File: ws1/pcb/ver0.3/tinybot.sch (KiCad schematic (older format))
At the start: 20 parts, among them IC1 ATTINY84-P, P1 PWR, P2 Pin Breakout, P3 ICSP, P4 M1, P5 M2, U1 LD1117S33TR, U2 L293D

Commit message: switching to DRV8835
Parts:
- removed U2: L293D, Housings_SOIC:SOIC-16_7.5x10.3mm_Pitch1.27mm, symbol L293D
- added U?: DRV8835, symbol DRV8835
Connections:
- net labels added: MODE, PH1, PH2
- wire segments 110 -> 92
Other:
- note added: "DRV8835 disconnect jumper."
- note removed: "L293D disconnect jumper."
- moved on the sheet: JP2, P3, P4, P5

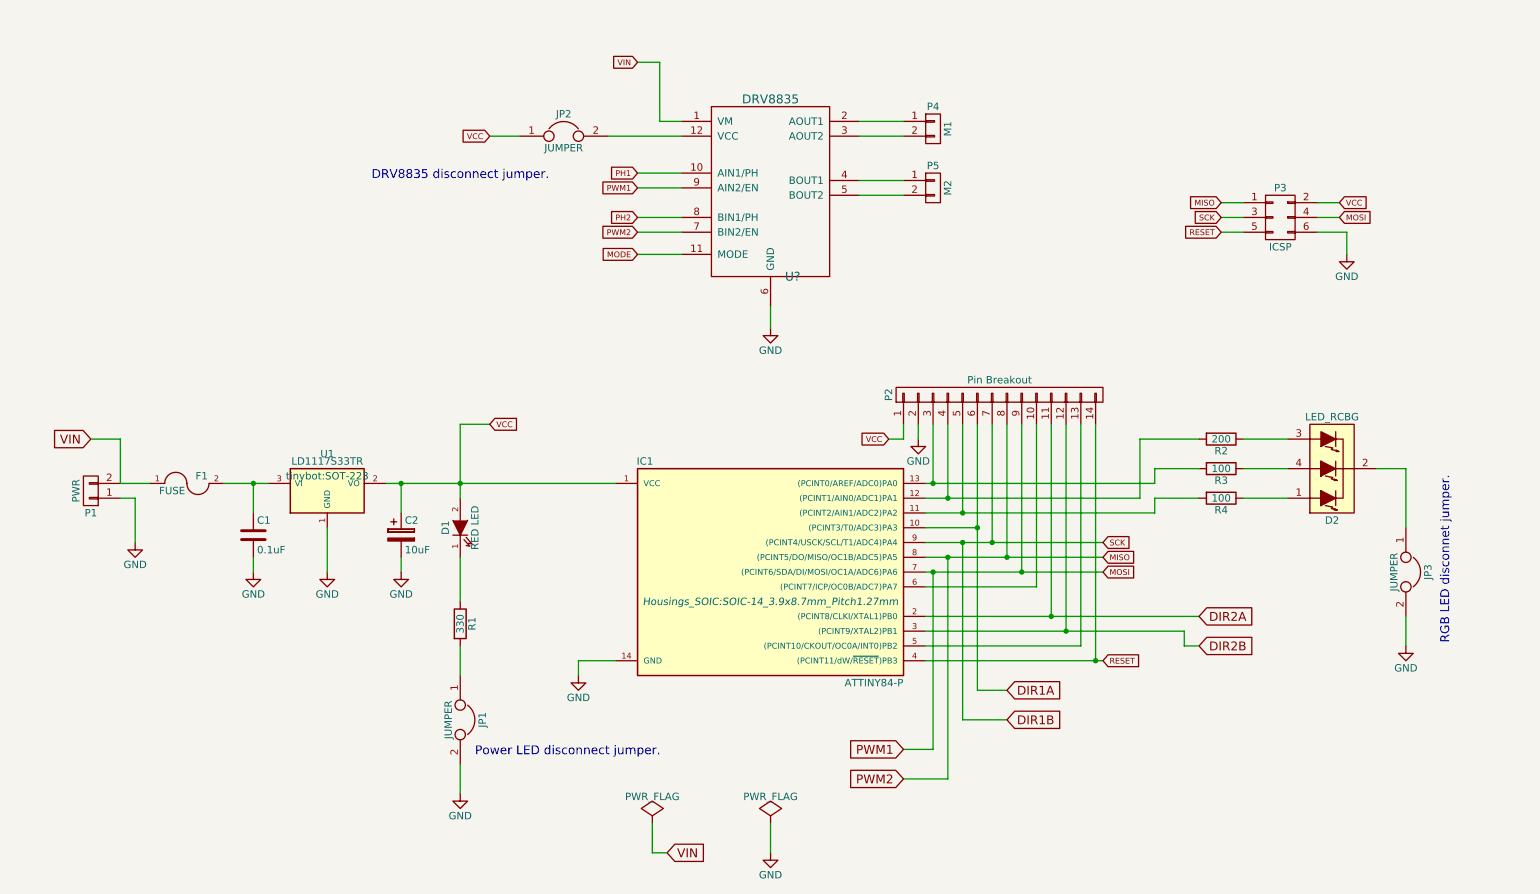
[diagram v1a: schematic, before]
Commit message: switching to DRV8835 and qfn
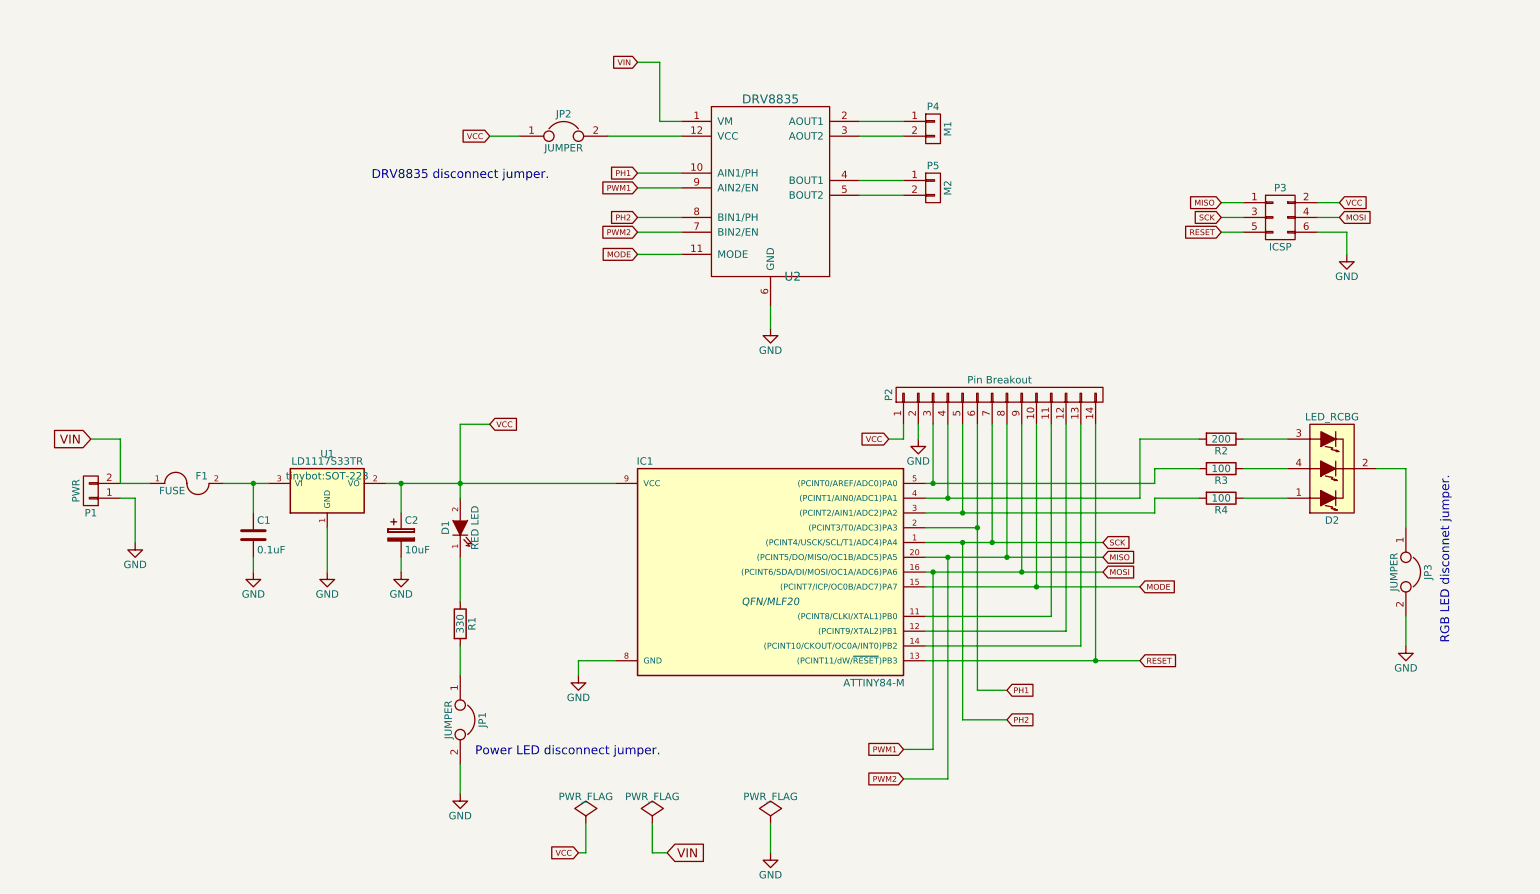
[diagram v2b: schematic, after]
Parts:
- removed IC1: ATTINY84-P, Housings_SOIC:SOIC-14_3.9x8.7mm_Pitch1.27mm, symbol ATTINY84-P
- added IC1: ATTINY84-M, QFN/MLF20, symbol ATTINY84-M
- U2: renamed from U?; footprint (none) -> tinybot:DRV8835
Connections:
- net DIR1A is gone; now on net PH1: P2.6 (P6)
- net DIR1B is gone; now on net PH2: P2.7 (P7), P3.3 (P3)
- net GND: now also IC1.8 (GND)
- net MISO: now also IC1.20 ((PCINT5/DO/MISO/OC1B/ADC5)PA5)
- net MODE: now also P2.10 (P10), IC1.15 ((PCINT7/ICP/OC0B/ADC7)PA7)
- net MOSI: now also IC1.16 ((PCINT6/SDA/DI/MOSI/OC1A/ADC6)PA6)
- net PH1: now also IC1.2 ((PCINT3/T0/ADC3)PA3)
- net PH2: now also IC1.1 ((PCINT4/USCK/SCL/T1/ADC4)PA4)
- net RESET: now also IC1.13 ((PCINT11/dW/~RESET~)PB3)
- net VCC: now also IC1.9 (VCC)
- net at P2.5 (P5), R4.2: now also IC1.3 ((PCINT2/AIN1/ADC2)PA2)
- net at P2.4 (P4), R2.2: now also IC1.4 ((PCINT1/AIN0/ADC1)PA1)
- net at P2.3 (P3), R3.2: now also IC1.5 ((PCINT0/AREF/ADC0)PA0)
- net at P2.13 (P13): now also IC1.14 ((PCINT10/CKOUT/OC0A/INT0)PB2)
- net DIR2A: no longer names the net of P2.11 (P11)
- net DIR2A: now also IC1.11 ((PCINT8/CLKI/XTAL1)PB0)
- net DIR2B: no longer names the net of P2.12 (P12)
- net DIR2B: now also IC1.12 ((PCINT9/XTAL2)PB1)
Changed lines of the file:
@@
 $EndDescr
-$Comp
-L ATTINY84-P IC1
-U 1 1 56DB9101
-P 5700 4600
-F 0 "IC1" H 4850 5350 50  0000 C CNN
-F 1 "ATTINY84-P" H 6400 3850 50  0000 C CNN
-F 2 "Housings_SOIC:SOIC-14_3.9x8.7mm_Pitch1.27mm" H 5700 4400 50  0000 C CIN
-F 3 "" H 5700 4600 50  0000 C CNN
-	1    5700 4600
-	1    0    0    -1
-$EndComp
 $Comp
 L LED D1
@@
 $EndComp
 $Comp
-L GND #PWR01
+L GND #PWR8
 U 1 1 56DBB7D0
 P 5700 6500
-F 0 "#PWR01" H 5700 6250 50  0001 C CNN
+F 0 "#PWR8" H 5700 6250 50  0001 C CNN
 F 1 "GND" H 5700 6350 50  0000 C CNN
 F 2 "" H 5700 6500 50  0000 C CNN
@@
 $EndComp
 $Comp
-L PWR_FLAG #FLG02
+L PWR_FLAG #FLG3
 U 1 1 56DBB7F9
 P 5700 6300
-F 0 "#FLG02" H 5700 6395 50  0001 C CNN
+F 0 "#FLG3" H 5700 6395 50  0001 C CNN
 F 1 "PWR_FLAG" H 5700 6480 50  0000 C CNN
 F 2 "" H 5700 6300 50  0000 C CNN
@@
 $EndComp
 $Comp
-L GND #PWR03
+L GND #PWR1
 U 1 1 56DBBFEE
 P 1400 4400
-F 0 "#PWR03" H 1400 4150 50  0001 C CNN
+F 0 "#PWR1" H 1400 4150 50  0001 C CNN
 F 1 "GND" H 1400 4250 50  0000 C CNN
 F 2 "" H 1400 4400 50  0000 C CNN
@@
 VIN
 $Comp
-L GND #PWR04
+L GND #PWR5
 U 1 1 56DBC175
 P 3600 6100
-F 0 "#PWR04" H 3600 5850 50  0001 C CNN
+F 0 "#PWR5" H 3600 5850 50  0001 C CNN
 F 1 "GND" H 3600 5950 50  0000 C CNN
 F 2 "" H 3600 6100 50  0000 C CNN
@@
 $EndComp
 $Comp
-L GND #PWR05
+L GND #PWR6
 U 1 1 56DBCAAD
 P 4400 5300
-F 0 "#PWR05" H 4400 5050 50  0001 C CNN
+F 0 "#PWR6" H 4400 5050 50  0001 C CNN
 F 1 "GND" H 4400 5150 50  0000 C CNN
 F 2 "" H 4400 5300 50  0000 C CNN
@@
 $EndComp
 $Comp
-L GND #PWR06
+L GND #PWR3
 U 1 1 56DBCBAE
 P 2700 4600
-F 0 "#PWR06" H 2700 4350 50  0001 C CNN
+F 0 "#PWR3" H 2700 4350 50  0001 C CNN
 F 1 "GND" H 2700 4450 50  0000 C CNN
 F 2 "" H 2700 4600 50  0000 C CNN
@@
 Text GLabel 7950 4600 2    39   Input ~ 0
 MOSI
-Text GLabel 7950 5200 2    39   Input ~ 0
+Text GLabel 8200 5200 2    39   Input ~ 0
 RESET
 Text GLabel 9550 2200 2    39   Input ~ 0
@@
 VCC
 $Comp
-L GND #PWR09
+L GND #PWR10
 U 1 1 56DBDDBC
 P 9600 2450
-F 0 "#PWR09" H 9600 2200 50  0001 C CNN
+F 0 "#PWR10" H 9600 2200 50  0001 C CNN
 F 1 "GND" H 9600 2300 50  0000 C CNN
 F 2 "" H 9600 2450 50  0000 C CNN
@@
 Text Notes 3000 1950 0    60   ~ 0
 DRV8835 disconnect jumper.
-Text GLabel 6600 5800 0    60   Input ~ 0
+Text GLabel 6600 5800 0    39   Input ~ 0
 PWM1
-Text GLabel 6600 6000 0    60   Input ~ 0
+Text GLabel 6600 6000 0    39   Input ~ 0
 PWM2
-Text GLabel 7300 5400 2    60   Input ~ 0
-DIR1A
-Text GLabel 7300 5600 2    60   Input ~ 0
-DIR1B
-Text GLabel 8600 4900 2    60   Input ~ 0
-DIR2A
-Text GLabel 8600 5100 2    60   Input ~ 0
-DIR2B
+Text GLabel 7300 5400 2    39   Input ~ 0
+PH1
+Text GLabel 7300 5600 2    39   Input ~ 0
+PH2
 $Comp
 L C C1
@@
 $EndComp
 $Comp
-L GND #PWR010
+L GND #PWR2
 U 1 1 56DC0DFE
 P 2200 4600
-F 0 "#PWR010" H 2200 4350 50  0001 C CNN
+F 0 "#PWR2" H 2200 4350 50  0001 C CNN
 F 1 "GND" H 2200 4450 50  0000 C CNN
 F 2 "" H 2200 4600 50  0000 C CNN
@@
 $EndComp
 $Comp
-L GND #PWR011
+L GND #PWR4
 U 1 1 56DC0E3F
 P 3200 4600
-F 0 "#PWR011" H 3200 4350 50  0001 C CNN
+F 0 "#PWR4" H 3200 4350 50  0001 C CNN
 F 1 "GND" H 3200 4450 50  0000 C CNN
 F 2 "" H 3200 4600 50  0000 C CNN
@@
 $EndComp
 $Comp
-L GND #PWR012
+L GND #PWR11
 U 1 1 56DD94E5
 P 10000 5100
-F 0 "#PWR012" H 10000 4850 50  0001 C CNN
+F 0 "#PWR11" H 10000 4850 50  0001 C CNN
 F 1 "GND" H 10000 4950 50  0000 C CNN
 F 2 "" H 10000 5100 50  0000 C CNN
@@
 VCC
 $Comp
-L GND #PWR013
+L GND #PWR9
 U 1 1 56DDA4AD
 P 6700 3700
-F 0 "#PWR013" H 6700 3450 50  0001 C CNN
+F 0 "#PWR9" H 6700 3450 50  0001 C CNN
 F 1 "GND" H 6700 3550 50  0000 C CNN
 F 2 "" H 6700 3700 50  0000 C CNN
@@
 VIN
 $Comp
-L PWR_FLAG #FLG014
+L PWR_FLAG #FLG2
 U 1 1 56DE7431
 P 4900 6300
-F 0 "#FLG014" H 4900 6395 50  0001 C CNN
+F 0 "#FLG2" H 4900 6395 50  0001 C CNN
 F 1 "PWR_FLAG" H 4900 6480 50  0000 C CNN
 F 2 "" H 4900 6300 50  0000 C CNN
@@
 $EndComp
 $Comp
-L DRV8835 U?
+L DRV8835 U2
 U 1 1 56E103E7
 P 5700 1800
-F 0 "U?" H 5850 1000 60  0000 C CNN
+F 0 "U2" H 5850 1000 60  0000 C CNN
 F 1 "DRV8835" H 5700 2200 60  0000 C CNN
-F 2 "" H 5700 1800 60  0000 C CNN
+F 2 "tinybot:DRV8835" H 5700 1800 60  0001 C CNN
 F 3 "" H 5700 1800 60  0000 C CNN
 	1    5700 1800
@@
 	7800 3600 7800 5100
 Wire Wire Line
-	6750 5000 8500 5000
-Wire Wire Line
-	7700 3600 7700 5000
-Wire Wire Line
-	6750 4900 8600 4900
-Wire Wire Line
-	7600 3600 7600 4900
-Wire Wire Line
-	7500 4700 6750 4700
+	6750 5000 7700 5000
+Wire Wire Line
+	7700 5000 7700 3600
+Wire Wire Line
+	6750 4900 7600 4900
+Wire Wire Line
+	7600 4900 7600 3600
+Wire Wire Line
+	6750 4700 8200 4700
 Wire Wire Line
 	7500 3600 7500 4700
@@
 	3600 3600 3800 3600
 Wire Wire Line
-	6750 5200 7950 5200
+	6750 5200 8200 5200
 Wire Wire Line
 	6750 4400 7950 4400
@@
 	7100 5400 7300 5400
 Connection ~ 7100 4300
-Connection ~ 7600 4900
-Wire Wire Line
-	8500 5000 8500 5100
-Wire Wire Line
-	8500 5100 8600 5100
-Connection ~ 7700 5000
 Wire Wire Line
 	3200 4000 3200 4200
@@
 	4800 2450 5100 2450
 $Comp
-L GND #PWR?
+L GND #PWR7
 U 1 1 56E11C7E
 P 5700 2950
-F 0 "#PWR?" H 5700 2700 50  0001 C CNN
+F 0 "#PWR7" H 5700 2700 50  0001 C CNN
 F 1 "GND" H 5700 2800 50  0000 C CNN
 F 2 "" H 5700 2950 50  0000 C CNN
@@
 Wire Wire Line
 	4950 1550 5100 1550
+Connection ~ 7500 4700
+Text GLabel 8200 4700 2    39   Input ~ 0
+MODE
+$Comp
+L PWR_FLAG #FLG1
+U 1 1 56E1399D
+P 4450 6300
+F 0 "#FLG1" H 4450 6395 50  0001 C CNN
+F 1 "PWR_FLAG" H 4450 6480 50  0000 C CNN
+F 2 "" H 4450 6300 50  0000 C CNN
+F 3 "" H 4450 6300 50  0000 C CNN
+	1    4450 6300
+	1    0    0    -1
+$EndComp
+Text GLabel 4400 6500 0    39   Input ~ 0
+VCC
+Wire Wire Line
+	4450 6300 4450 6500
+Wire Wire Line
+	4450 6500 4400 6500
+$Comp
+L ATTINY84-M IC1
+U 1 1 56E154DB
+P 5700 4600
+F 0 "IC1" H 4850 5350 50  0000 C CNN
+F 1 "ATTINY84-M" H 6400 3850 50  0000 C CNN
+F 2 "QFN/MLF20" H 5700 4400 50  0000 C CIN
+F 3 "" H 5700 4600 50  0000 C CNN
+	1    5700 4600
+	1    0    0    -1
+$EndComp
 $EndSCHEMATC

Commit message: switching to DRV8835 and qfn
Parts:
- IC1: footprint QFN/MLF20 -> Housings_DFN_QFN:QFN-20-1EP_4x4mm_Pitch0.5mm
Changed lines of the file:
@@
 $EndComp
 $Comp
-L GND #PWR8
+L GND #PWR01
 U 1 1 56DBB7D0
 P 5700 6500
-F 0 "#PWR8" H 5700 6250 50  0001 C CNN
+F 0 "#PWR01" H 5700 6250 50  0001 C CNN
 F 1 "GND" H 5700 6350 50  0000 C CNN
 F 2 "" H 5700 6500 50  0000 C CNN
@@
 $EndComp
 $Comp
-L PWR_FLAG #FLG3
+L PWR_FLAG #FLG02
 U 1 1 56DBB7F9
 P 5700 6300
-F 0 "#FLG3" H 5700 6395 50  0001 C CNN
+F 0 "#FLG02" H 5700 6395 50  0001 C CNN
 F 1 "PWR_FLAG" H 5700 6480 50  0000 C CNN
 F 2 "" H 5700 6300 50  0000 C CNN
@@
 $EndComp
 $Comp
-L GND #PWR1
+L GND #PWR03
 U 1 1 56DBBFEE
 P 1400 4400
-F 0 "#PWR1" H 1400 4150 50  0001 C CNN
+F 0 "#PWR03" H 1400 4150 50  0001 C CNN
 F 1 "GND" H 1400 4250 50  0000 C CNN
 F 2 "" H 1400 4400 50  0000 C CNN
@@
 VIN
 $Comp
-L GND #PWR5
+L GND #PWR04
 U 1 1 56DBC175
 P 3600 6100
-F 0 "#PWR5" H 3600 5850 50  0001 C CNN
+F 0 "#PWR04" H 3600 5850 50  0001 C CNN
 F 1 "GND" H 3600 5950 50  0000 C CNN
 F 2 "" H 3600 6100 50  0000 C CNN
@@
 $EndComp
 $Comp
-L GND #PWR6
+L GND #PWR05
 U 1 1 56DBCAAD
 P 4400 5300
-F 0 "#PWR6" H 4400 5050 50  0001 C CNN
+F 0 "#PWR05" H 4400 5050 50  0001 C CNN
 F 1 "GND" H 4400 5150 50  0000 C CNN
 F 2 "" H 4400 5300 50  0000 C CNN
@@
 $EndComp
 $Comp
-L GND #PWR3
+L GND #PWR06
 U 1 1 56DBCBAE
 P 2700 4600
-F 0 "#PWR3" H 2700 4350 50  0001 C CNN
+F 0 "#PWR06" H 2700 4350 50  0001 C CNN
 F 1 "GND" H 2700 4450 50  0000 C CNN
 F 2 "" H 2700 4600 50  0000 C CNN
@@
 VCC
 $Comp
-L GND #PWR10
+L GND #PWR07
 U 1 1 56DBDDBC
 P 9600 2450
-F 0 "#PWR10" H 9600 2200 50  0001 C CNN
+F 0 "#PWR07" H 9600 2200 50  0001 C CNN
 F 1 "GND" H 9600 2300 50  0000 C CNN
 F 2 "" H 9600 2450 50  0000 C CNN
@@
 $EndComp
 $Comp
-L GND #PWR2
+L GND #PWR08
 U 1 1 56DC0DFE
 P 2200 4600
-F 0 "#PWR2" H 2200 4350 50  0001 C CNN
+F 0 "#PWR08" H 2200 4350 50  0001 C CNN
 F 1 "GND" H 2200 4450 50  0000 C CNN
 F 2 "" H 2200 4600 50  0000 C CNN
@@
 $EndComp
 $Comp
-L GND #PWR4
+L GND #PWR09
 U 1 1 56DC0E3F
 P 3200 4600
-F 0 "#PWR4" H 3200 4350 50  0001 C CNN
+F 0 "#PWR09" H 3200 4350 50  0001 C CNN
 F 1 "GND" H 3200 4450 50  0000 C CNN
 F 2 "" H 3200 4600 50  0000 C CNN
@@
 $EndComp
 $Comp
-L GND #PWR11
+L GND #PWR010
 U 1 1 56DD94E5
 P 10000 5100
-F 0 "#PWR11" H 10000 4850 50  0001 C CNN
+F 0 "#PWR010" H 10000 4850 50  0001 C CNN
 F 1 "GND" H 10000 4950 50  0000 C CNN
 F 2 "" H 10000 5100 50  0000 C CNN
@@
 VCC
 $Comp
-L GND #PWR9
+L GND #PWR011
 U 1 1 56DDA4AD
 P 6700 3700
-F 0 "#PWR9" H 6700 3450 50  0001 C CNN
+F 0 "#PWR011" H 6700 3450 50  0001 C CNN
 F 1 "GND" H 6700 3550 50  0000 C CNN
 F 2 "" H 6700 3700 50  0000 C CNN
@@
 VIN
 $Comp
-L PWR_FLAG #FLG2
+L PWR_FLAG #FLG012
 U 1 1 56DE7431
 P 4900 6300
-F 0 "#FLG2" H 4900 6395 50  0001 C CNN
+F 0 "#FLG012" H 4900 6395 50  0001 C CNN
 F 1 "PWR_FLAG" H 4900 6480 50  0000 C CNN
 F 2 "" H 4900 6300 50  0000 C CNN
@@
 	4800 2450 5100 2450
 $Comp
-L GND #PWR7
+L GND #PWR013
 U 1 1 56E11C7E
 P 5700 2950
-F 0 "#PWR7" H 5700 2700 50  0001 C CNN
+F 0 "#PWR013" H 5700 2700 50  0001 C CNN
 F 1 "GND" H 5700 2800 50  0000 C CNN
 F 2 "" H 5700 2950 50  0000 C CNN
@@
 MODE
 $Comp
-L PWR_FLAG #FLG1
+L PWR_FLAG #FLG014
 U 1 1 56E1399D
 P 4450 6300
-F 0 "#FLG1" H 4450 6395 50  0001 C CNN
+F 0 "#FLG014" H 4450 6395 50  0001 C CNN
 F 1 "PWR_FLAG" H 4450 6480 50  0000 C CNN
 F 2 "" H 4450 6300 50  0000 C CNN
@@
 F 0 "IC1" H 4850 5350 50  0000 C CNN
 F 1 "ATTINY84-M" H 6400 3850 50  0000 C CNN
-F 2 "QFN/MLF20" H 5700 4400 50  0000 C CIN
+F 2 "Housings_DFN_QFN:QFN-20-1EP_4x4mm_Pitch0.5mm" H 5700 4400 50  0000 C CIN
 F 3 "" H 5700 4600 50  0000 C CNN
 	1    5700 4600

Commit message: added mosfet
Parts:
- added Q1: NCE3407A, TO_SOT_Packages_SMD:SOT-23, symbol P_MOS
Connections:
- net GND: now also Q1.1 (G)
- net at C1.1, U1.3 (VI): now also Q1.2 (S); no longer F1.2
- new net: F1.2, Q1.3 (D)
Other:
- moved on the sheet: C1, C2, D1, D2, F1, IC1, JP1, JP3, P1, P2, R1, R2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

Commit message: updated schematic and pcb added mounting holes
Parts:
- added C3: 0.1uF, Capacitors_SMD:C_0603, symbol C
- added C4: 10uF, Capacitors_SMD:C_0603, symbol C
- added SW1: SW_PUSH, tinybot:SWITCH_SKQGAKE010, symbol SW_PUSH
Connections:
- net GND: now also C3.2, C4.2, SW1.2
- net RESET: now also SW1.1
- net VCC: now also C3.1
- net VIN: now also C4.1
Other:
- note added: "Press to reset."
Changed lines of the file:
@@
 	1    0    0    -1
 $EndComp
-Text Notes 3000 1950 0    60   ~ 0
+Text Notes 3050 1450 0    60   ~ 0
 DRV8835 disconnect jumper.
 Text GLabel 7100 5700 0    39   Input ~ 0
@@
 	1    0    0    -1
 $EndComp
-Text GLabel 4800 1150 0    39   Input ~ 0
+Text GLabel 4550 850  0    39   Input ~ 0
 VIN
 Text GLabel 8700 4600 2    39   Input ~ 0
@@
 Connection ~ 8400 5100
 Wire Wire Line
-	8400 3500 8400 5100
+	8400 3500 8400 5600
 Wire Wire Line
 	8300 5000 7250 5000
@@
 	4600 1650 5100 1650
 Wire Wire Line
-	4800 1150 4950 1150
-Wire Wire Line
-	4950 1150 4950 1550
+	4950 850  4950 1550
 Wire Wire Line
 	4950 1550 5100 1550
@@
 Wire Wire Line
 	2350 4200 2350 4500
+$Comp
+L SW_PUSH SW1
+U 1 1 56E2ABAC
+P 8900 5600
+F 0 "SW1" H 9050 5710 50  0000 C CNN
+F 1 "SW_PUSH" H 8900 5520 50  0000 C CNN
+F 2 "tinybot:SWITCH_SKQGAKE010" H 8900 5600 50  0001 C CNN
+F 3 "" H 8900 5600 50  0000 C CNN
+	1    8900 5600
+	1    0    0    -1
+$EndComp
+Wire Wire Line
+	8400 5600 8600 5600
+$Comp
+L GND #PWR016
+U 1 1 56E2AD64
+P 9400 5700
+F 0 "#PWR016" H 9400 5450 50  0001 C CNN
+F 1 "GND" H 9400 5550 50  0000 C CNN
+F 2 "" H 9400 5700 50  0000 C CNN
+F 3 "" H 9400 5700 50  0000 C CNN
+	1    9400 5700
+	1    0    0    -1
+$EndComp
+Wire Wire Line
+	9200 5600 9400 5600
+Wire Wire Line
+	9400 5600 9400 5700
+Text Notes 8600 5900 0    60   ~ 0
+Press to reset.
+$Comp
+L C C3
+U 1 1 56E2B2C0
+P 3900 2000
+F 0 "C3" H 3925 2100 50  0000 L CNN
+F 1 "0.1uF" H 3925 1900 50  0000 L CNN
+F 2 "Capacitors_SMD:C_0603" H 3938 1850 50  0001 C CNN
+F 3 "" H 3900 2000 50  0000 C CNN
+	1    3900 2000
+	1    0    0    -1
+$EndComp
+$Comp
+L C C4
+U 1 1 56E2B323
+P 4700 1050
+F 0 "C4" H 4725 1150 50  0000 L CNN
+F 1 "10uF" H 4725 950 50  0000 L CNN
+F 2 "Capacitors_SMD:C_0603" H 4738 900 50  0001 C CNN
+F 3 "" H 4700 1050 50  0000 C CNN
+	1    4700 1050
+	1    0    0    -1
+$EndComp
+$Comp
+L GND #PWR017
+U 1 1 56E2B728
+P 3900 2300
+F 0 "#PWR017" H 3900 2050 50  0001 C CNN
+F 1 "GND" H 3900 2150 50  0000 C CNN
+F 2 "" H 3900 2300 50  0000 C CNN
+F 3 "" H 3900 2300 50  0000 C CNN
+	1    3900 2300
+	1    0    0    -1
+$EndComp
+$Comp
+L GND #PWR018
+U 1 1 56E2B77B
+P 4700 1300
+F 0 "#PWR018" H 4700 1050 50  0001 C CNN
+F 1 "GND" H 4700 1150 50  0000 C CNN
+F 2 "" H 4700 1300 50  0000 C CNN
+F 3 "" H 4700 1300 50  0000 C CNN
+	1    4700 1300
+	1    0    0    -1
+$EndComp
+Wire Wire Line
+	4550 850  4950 850
+Wire Wire Line
+	4700 900  4700 850
+Connection ~ 4700 850
+Wire Wire Line
+	4700 1200 4700 1300
+Wire Wire Line
+	3900 1850 3900 1650
+Connection ~ 3900 1650
+Wire Wire Line
+	3900 2150 3900 2300
 $EndSCHEMATC
